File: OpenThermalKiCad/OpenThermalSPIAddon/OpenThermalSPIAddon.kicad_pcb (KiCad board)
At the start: 2 copper layers, 78.7 x 81.3 mm, 3 parts

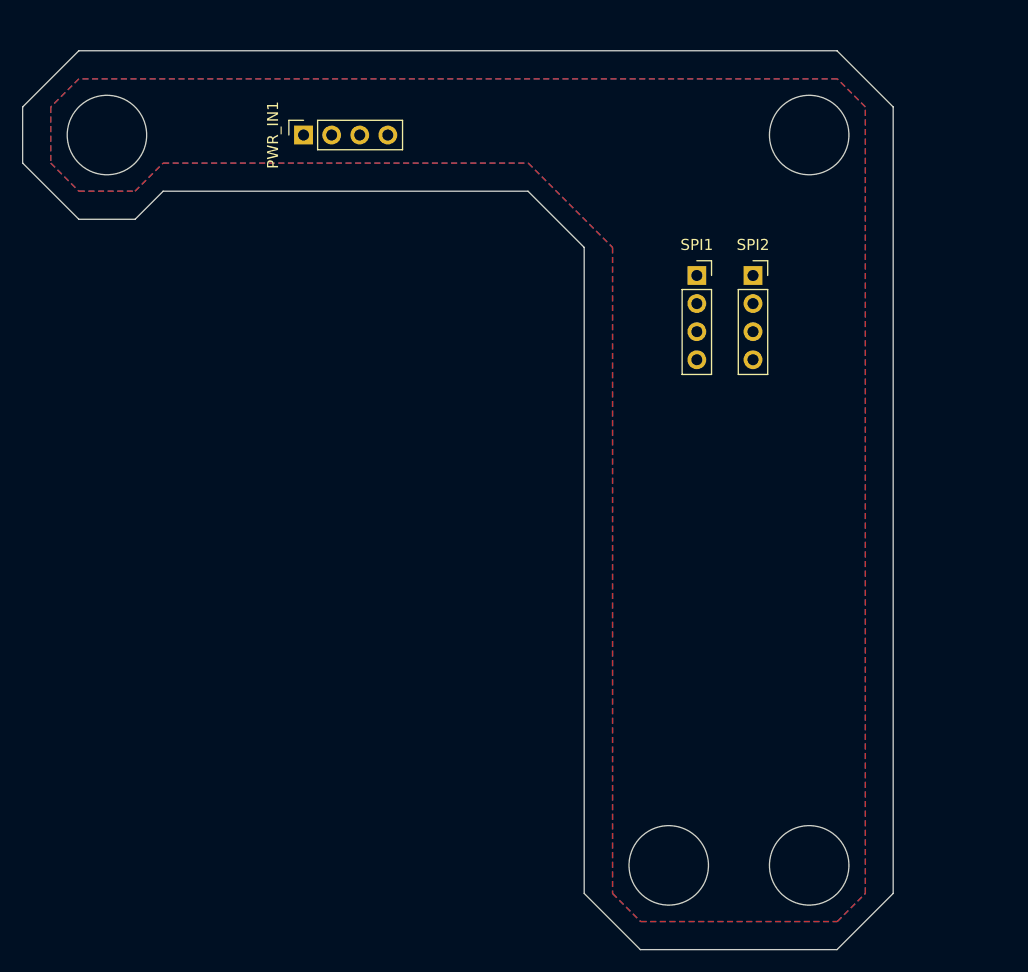
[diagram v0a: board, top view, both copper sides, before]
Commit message: Updated wiring + components
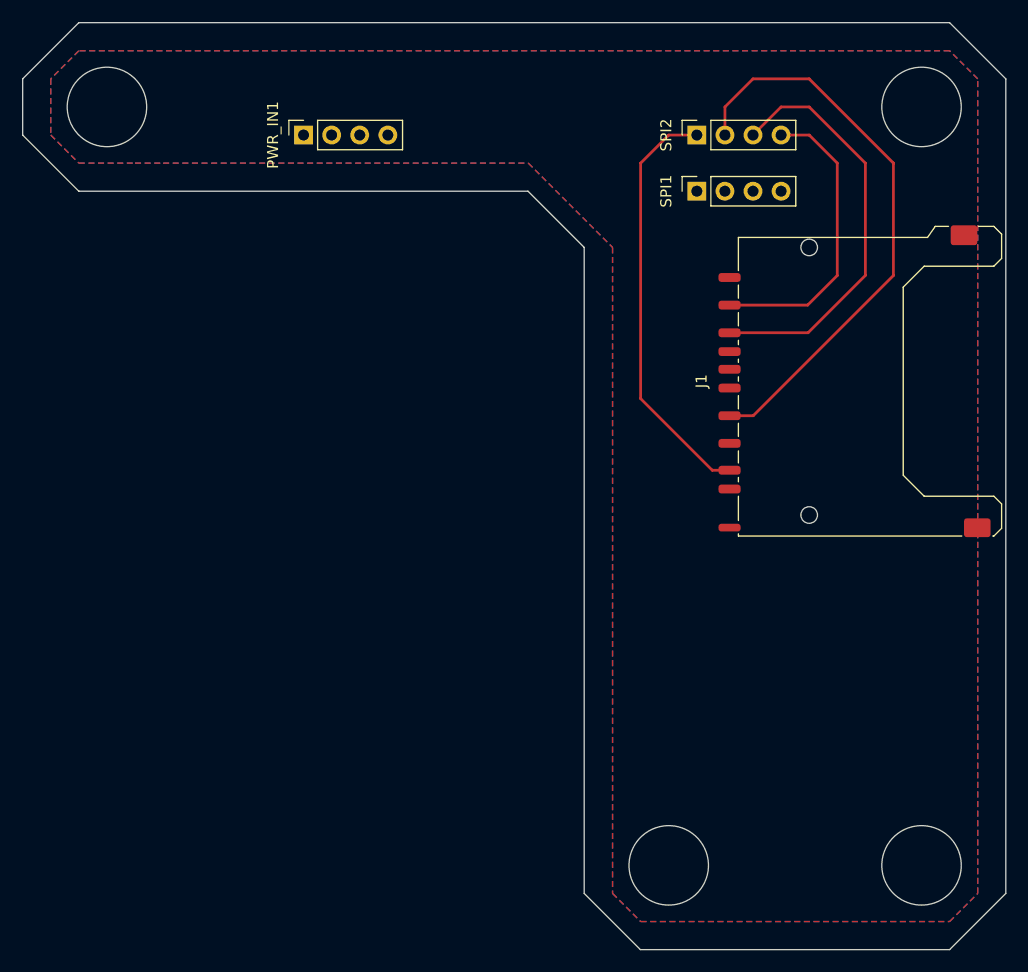
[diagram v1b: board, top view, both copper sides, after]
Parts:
- added J1: SD_Card, Connector_Card:SD_Kyocera_145638009211859+, F.Cu at (94.2, 47.7)
- moved SPI2 13.7 mm to (78.7, 25.4), turned to 90 degrees
- moved SPI1 7.62 mm to (78.7, 30.5), turned to 90 degrees
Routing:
- net SPI2_CLOCK: track 0.00 -> 52.2 mm
- net SPI2_MISO: track 0.00 -> 38.1 mm
- net SPI2_MOSI: track 0.00 -> 37.9 mm
- net SPI2_CS: track 0.00 -> 27.1 mm
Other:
- board size 78.7 x 81.3 mm -> 88.9 x 83.8 mm
